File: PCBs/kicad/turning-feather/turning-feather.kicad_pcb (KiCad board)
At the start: 2 copper layers, 64.8 x 72.4 mm, 24 parts, among them J1 Out to power switch, J2 Out to RJ45, J3 Buttons/beep, J4 RJ45_Shielded, J5 Spare, U1 TSR 1-2450, U2 MIC4427, U3 MIC4427, U4 ZPT

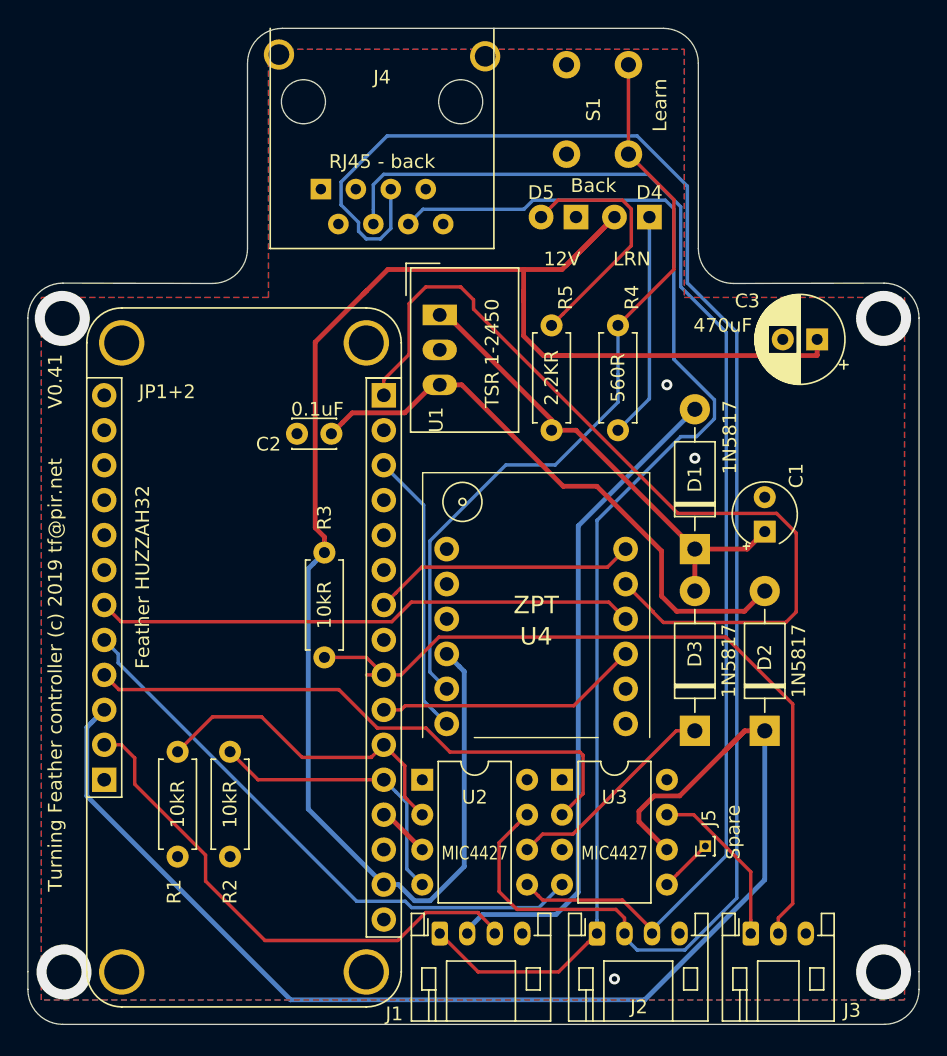
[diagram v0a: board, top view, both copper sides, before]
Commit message: Move DIL base slightly over to provide room for header sockets to be used
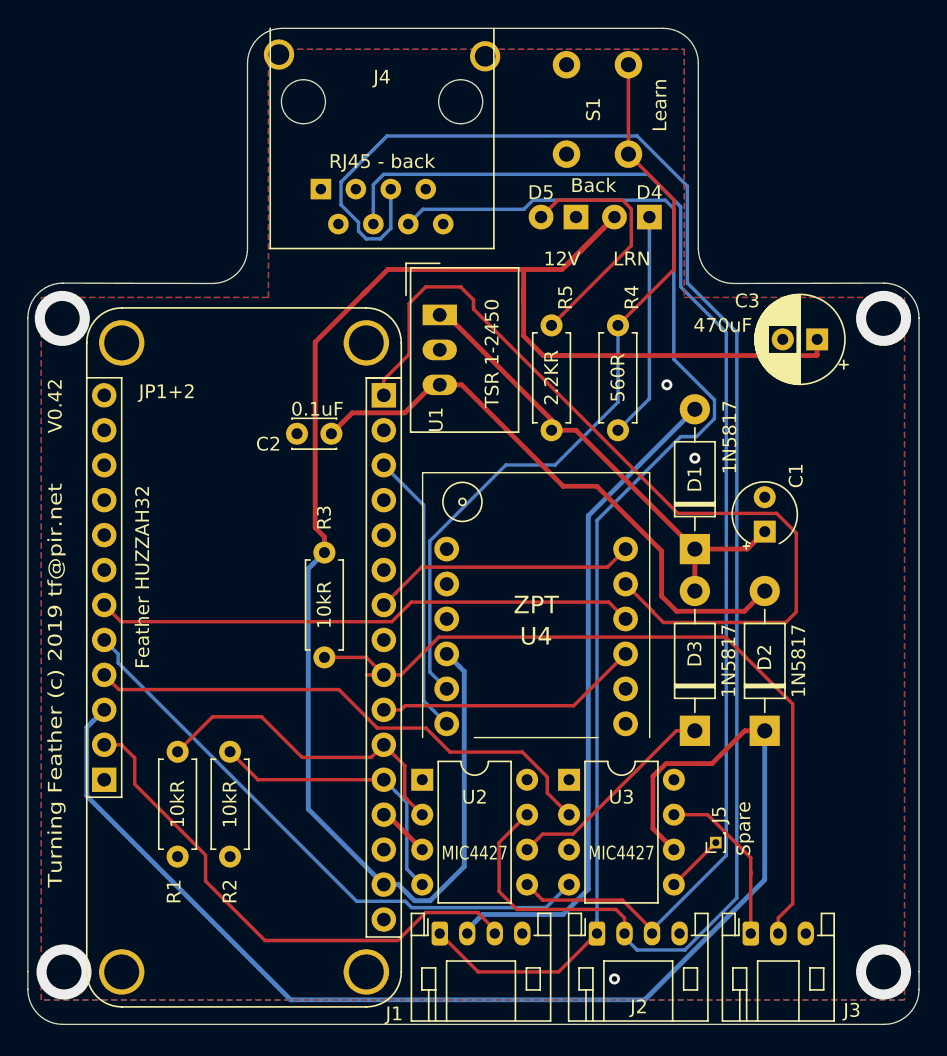
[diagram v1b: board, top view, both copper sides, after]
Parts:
- moved J5 0.80 mm to (154.7, 153.7)
- moved U3 0.51 mm to (144.0, 149.1)
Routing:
- net Net-(JP1+2-Pad25): track 42.2 -> 38.7 mm
- net +5V: track 93.9 -> 92.1 mm
- net Net-(JP1+2-Pad24): track 42.4 -> 43.6 mm
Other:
- board text added: "Turning Feather (c) 2019 tf@pir.net"
- board text added: "V0.42"
- board text removed: "Turning Feather controller (c) 2019 tf@pir.net"
- board text removed: "V0.41"
